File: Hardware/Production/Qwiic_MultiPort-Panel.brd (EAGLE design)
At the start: 149.1 x 143.3 mm, 606 parts, among them J1 QWIIC_RIGHT_ANGLE, J10 QWIIC_RIGHT_ANGLE, J100 QWIIC_RIGHT_ANGLE, J11 QWIIC_RIGHT_ANGLE, J12 QWIIC_RIGHT_ANGLE, J13 QWIIC_RIGHT_ANGLE, J14 QWIIC_RIGHT_ANGLE, J15 QWIIC_RIGHT_ANGLE, J16 QWIIC_RIGHT_ANGLE, J17 QWIIC_RIGHT_ANGLE, J18 QWIIC_RIGHT_ANGLE, J19 QWIIC_RIGHT_ANGLE, J2 QWIIC_RIGHT_ANGLE, J20 QWIIC_RIGHT_ANGLE, J21 QWIIC_RIGHT_ANGLE, J22 QWIIC_RIGHT_ANGLE, J23 QWIIC_RIGHT_ANGLE, J24 QWIIC_RIGHT_ANGLE, J25 QWIIC_RIGHT_ANGLE, J26 QWIIC_RIGHT_ANGLE, J27 QWIIC_RIGHT_ANGLE, J28 QWIIC_RIGHT_ANGLE, J29 QWIIC_RIGHT_ANGLE, J3 QWIIC_RIGHT_ANGLE, J30 QWIIC_RIGHT_ANGLE, J31 QWIIC_RIGHT_ANGLE, J32 QWIIC_RIGHT_ANGLE, J33 QWIIC_RIGHT_ANGLE, J34 QWIIC_RIGHT_ANGLE, J35 QWIIC_RIGHT_ANGLE, J36 QWIIC_RIGHT_ANGLE, J37 QWIIC_RIGHT_ANGLE, J38 QWIIC_RIGHT_ANGLE, J39 QWIIC_RIGHT_ANGLE, J4 QWIIC_RIGHT_ANGLE, J40 QWIIC_RIGHT_ANGLE, J41 QWIIC_RIGHT_ANGLE, J42 QWIIC_RIGHT_ANGLE, J43 QWIIC_RIGHT_ANGLE, J44 QWIIC_RIGHT_ANGLE, J45 QWIIC_RIGHT_ANGLE, J46 QWIIC_RIGHT_ANGLE, J47 QWIIC_RIGHT_ANGLE, J48 QWIIC_RIGHT_ANGLE, J49 QWIIC_RIGHT_ANGLE, J5 QWIIC_RIGHT_ANGLE, J50 QWIIC_RIGHT_ANGLE, J51 QWIIC_RIGHT_ANGLE, J52 QWIIC_RIGHT_ANGLE, J53 QWIIC_RIGHT_ANGLE, J54 QWIIC_RIGHT_ANGLE, J55 QWIIC_RIGHT_ANGLE, J56 QWIIC_RIGHT_ANGLE, J57 QWIIC_RIGHT_ANGLE, J58 QWIIC_RIGHT_ANGLE, J59 QWIIC_RIGHT_ANGLE, J6 QWIIC_RIGHT_ANGLE, J60 QWIIC_RIGHT_ANGLE, J61 QWIIC_RIGHT_ANGLE, J62 QWIIC_RIGHT_ANGLE, J63 QWIIC_RIGHT_ANGLE, J64 QWIIC_RIGHT_ANGLE, J65 QWIIC_RIGHT_ANGLE, J66 QWIIC_RIGHT_ANGLE, J67 QWIIC_RIGHT_ANGLE, J68 QWIIC_RIGHT_ANGLE, J69 QWIIC_RIGHT_ANGLE, J7 QWIIC_RIGHT_ANGLE, J70 QWIIC_RIGHT_ANGLE, J71 QWIIC_RIGHT_ANGLE, J72 QWIIC_RIGHT_ANGLE, J73 QWIIC_RIGHT_ANGLE, J74 QWIIC_RIGHT_ANGLE, J75 QWIIC_RIGHT_ANGLE, J76 QWIIC_RIGHT_ANGLE, J77 QWIIC_RIGHT_ANGLE, J78 QWIIC_RIGHT_ANGLE, J79 QWIIC_RIGHT_ANGLE, J8 QWIIC_RIGHT_ANGLE, J80 QWIIC_RIGHT_ANGLE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

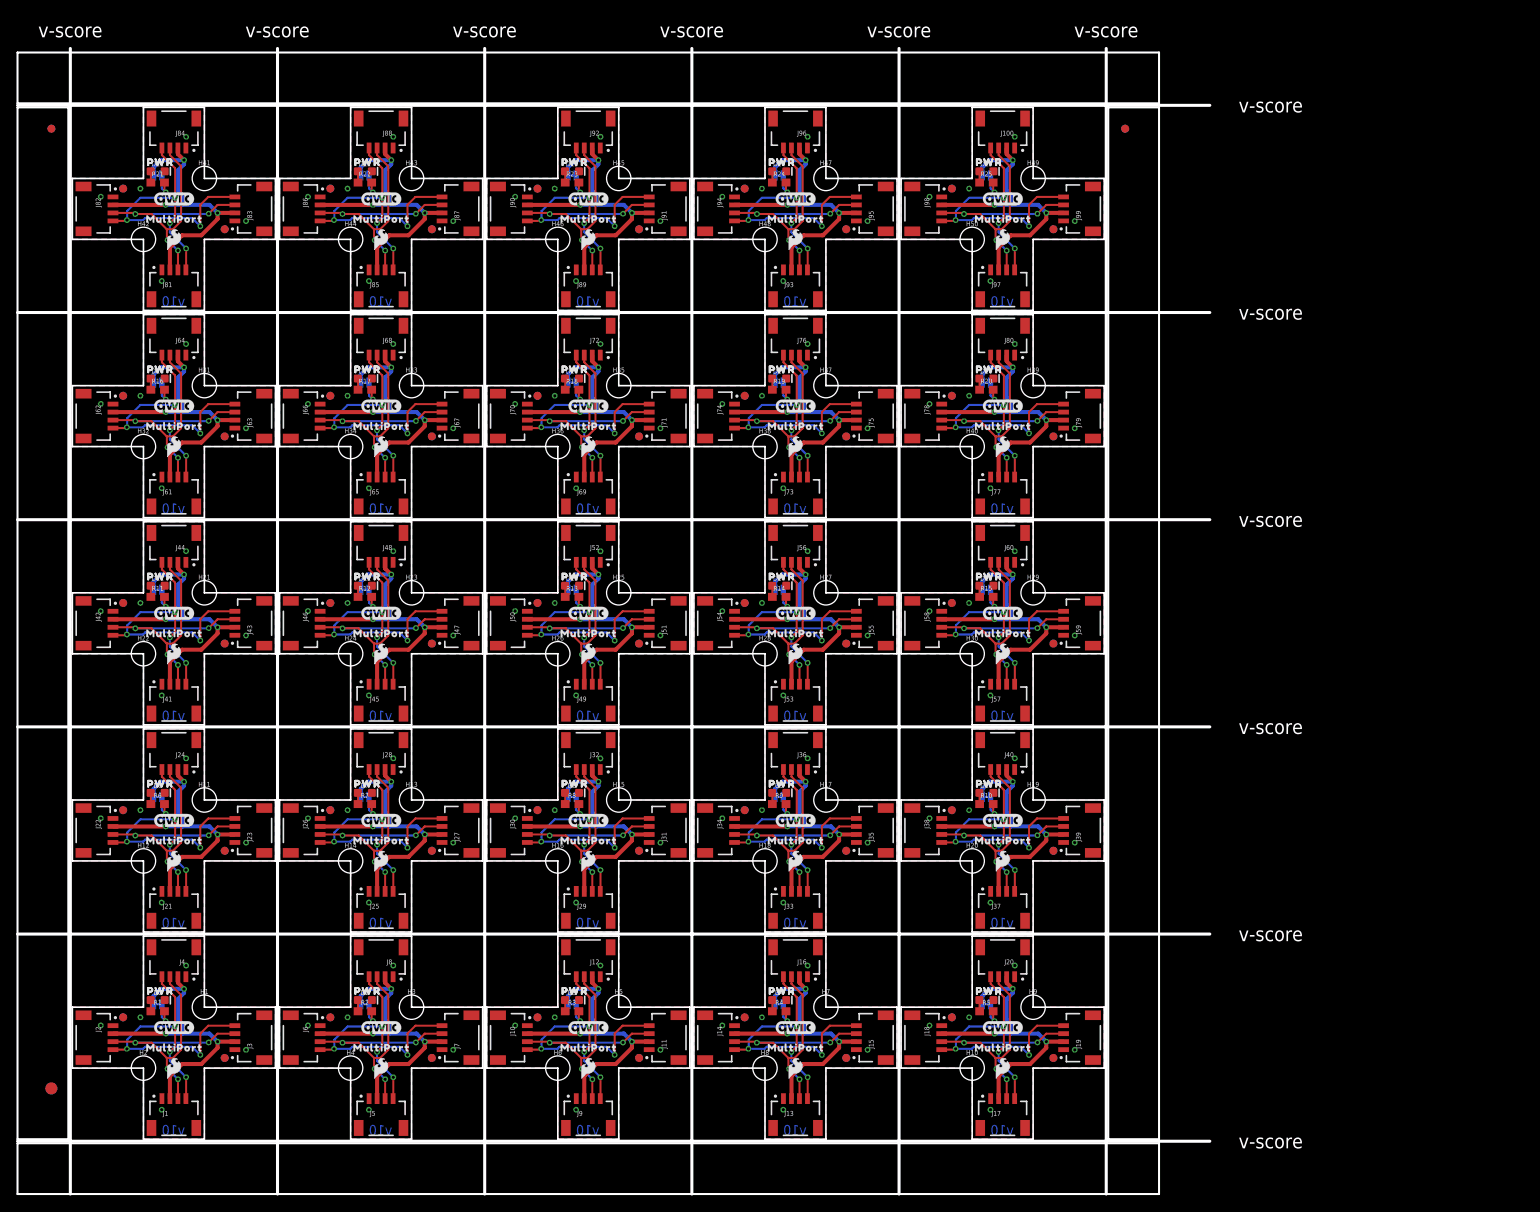
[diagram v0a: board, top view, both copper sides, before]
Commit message: MultiPort - re-panelized
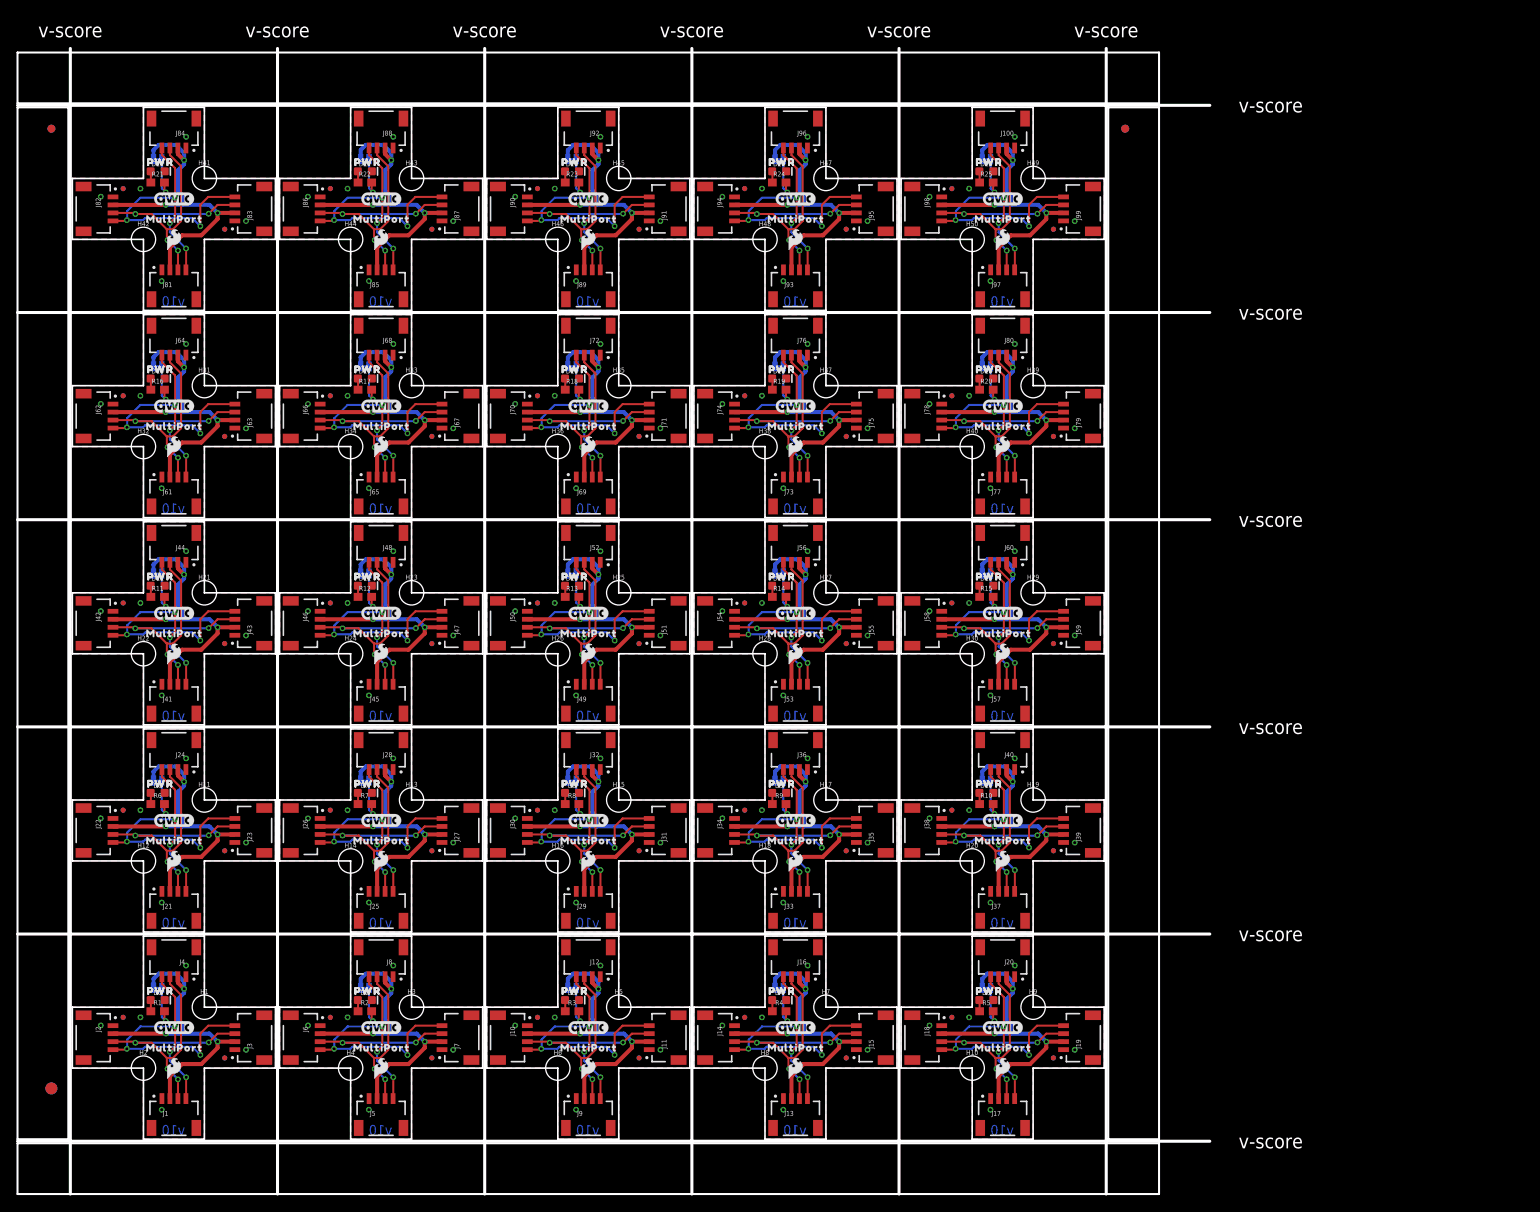
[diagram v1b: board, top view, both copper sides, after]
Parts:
- FD1, FD10, FD100, FD11, FD12, FD13, FD14, FD15, FD16, FD17, FD18, FD19, FD2, FD20, FD21, FD22, FD23, FD24, FD25, FD26, FD27, FD28, FD29, FD3, FD30, FD31, FD32, FD33, FD34, FD35, FD36, FD37, FD38, FD39, FD4, FD40, FD41, FD42, FD43, FD44, FD45, FD46, FD47, FD48, FD49, FD5, FD50, FD51, FD52, FD53, FD54, FD55, FD56, FD57, FD58, FD59, FD6, FD60, FD61, FD62, FD63, FD64, FD65, FD66, FD67, FD68, FD69, FD7, FD70, FD71, FD72, FD73, FD74, FD75, FD76, FD77, FD78, FD79, FD8, FD80, FD81, FD82, FD83, FD84, FD85, FD86, FD87, FD88, FD89, FD9, FD90, FD91, FD92, FD93, FD94, FD95, FD96, FD97, FD98, FD99: value FIDUCIAL1X2 -> FIDUCIALUFIDUCIAL; device SparkFun-Aesthetics:FIDUCIAL-1X2 -> SparkFun-Aesthetics:FIDUCIAL-MICRO
- U$104, U$111, U$118, U$12, U$125, U$132, U$139, U$146, U$153, U$160, U$167, U$174, U$20, U$27, U$34, U$41, U$48, U$55, U$62, U$69, U$76, U$83, U$90, U$97: device output:PWR0 -> output:MULTIPORT0
- U$105, U$112, U$119, U$126, U$133, U$14, U$140, U$147, U$154, U$161, U$168, U$175, U$21, U$28, U$35, U$42, U$49, U$56, U$63, U$70, U$77, U$84, U$91, U$98: device output:MULTIPORT0 -> output:#PWR#0
- U$3: device output:PWR0 -> SparkFun-Aesthetics:SFE_LOGO_FLAME_.1
- U$5: device SparkFun-Aesthetics:SFE_LOGO_FLAME_.1 -> output:#PWR#0
- moved U$3 27.4 mm to (38.6, 8.89), flipped to the top
- moved U$5 25.1 mm to (15.6, 18.9), flipped to the bottom
- moved U$119 10.3 mm to (41.5, 96.6), flipped to the bottom
- moved U$154 10.3 mm to (41.5, 122.6), flipped to the bottom
- moved U$112 10.3 mm to (15.6, 96.6), flipped to the bottom
- moved U$147 10.3 mm to (15.6, 122.6), flipped to the bottom
- moved U$126 10.3 mm to (67.4, 96.6), flipped to the bottom
- moved U$133 10.3 mm to (93.3, 96.6), flipped to the bottom
- moved U$140 10.3 mm to (119.3, 96.6), flipped to the bottom
- moved U$161 10.3 mm to (67.4, 122.6), flipped to the bottom
- moved U$168 10.3 mm to (93.3, 122.6), flipped to the bottom
- moved U$175 10.3 mm to (119.3, 122.6), flipped to the bottom
- moved U$49 10.3 mm to (41.5, 44.8), flipped to the bottom
- moved U$84 10.3 mm to (41.5, 70.7), flipped to the bottom
- moved U$42 10.3 mm to (15.6, 44.8), flipped to the bottom
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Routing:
- net N$50: track 3.63 -> 5.66 mm
- net N$48: track 3.63 -> 5.66 mm
- net N$46: track 3.63 -> 5.66 mm
- net N$44: track 3.63 -> 5.66 mm
- net N$42: track 3.63 -> 5.66 mm
- net N$40: track 3.63 -> 5.66 mm
- net N$38: track 3.63 -> 5.66 mm
- net N$36: track 3.63 -> 5.66 mm
- net N$34: track 3.63 -> 5.66 mm
- net N$32: track 3.63 -> 5.66 mm
- net N$30: track 3.63 -> 5.66 mm
- net N$28: track 3.63 -> 5.66 mm
- net N$26: track 3.63 -> 5.66 mm
- net N$24: track 3.63 -> 5.66 mm
- net N$22: track 3.63 -> 5.66 mm
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
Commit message: Re-panelized Qwiic MultiPort
Less than 7x5 inches
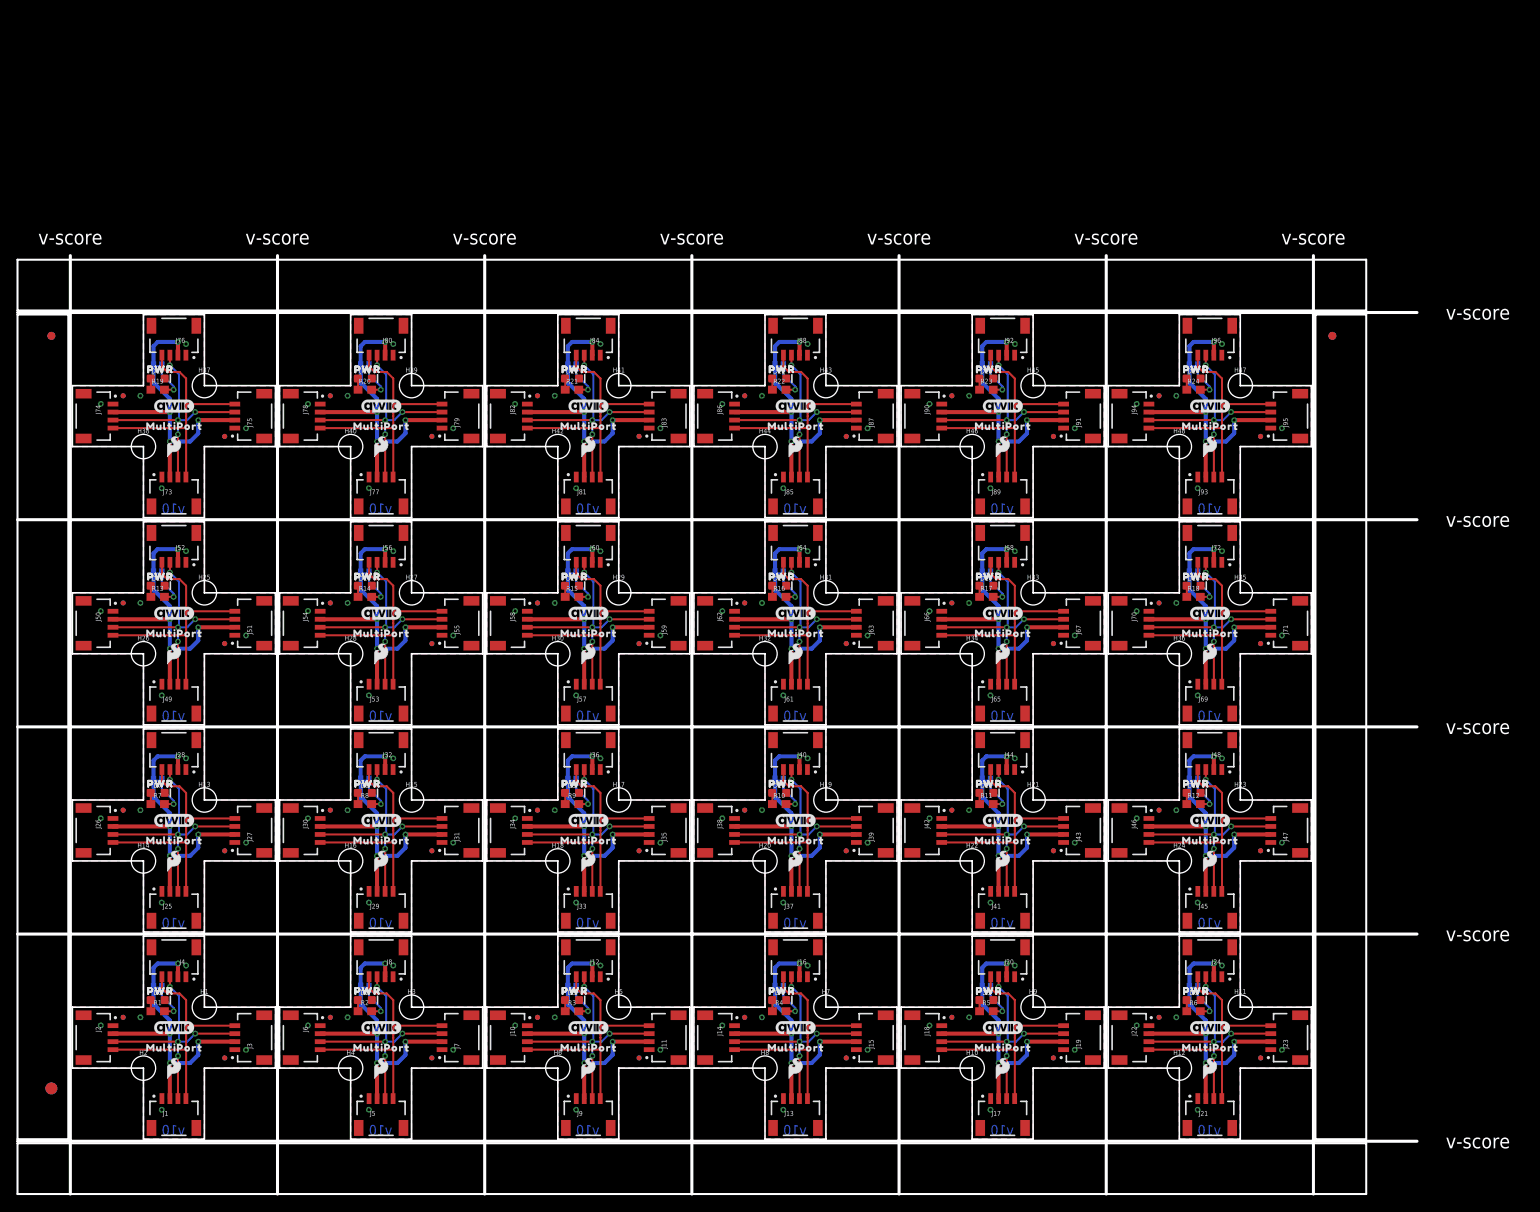
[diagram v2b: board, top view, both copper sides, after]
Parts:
- removed D25: RED, SparkFun-LED:LED-0603
- removed FD100, FD97, FD98, FD99: FIDUCIALUFIDUCIAL, SparkFun-Aesthetics:FIDUCIAL-MICRO
- removed H49, H50: STAND-OFFTIGHT, SparkFun-Hardware:STAND-OFF-TIGHT
- removed J100, J97, J98, J99: QWIIC_RIGHT_ANGLE, SparkFun-Connectors:JST04_1MM_RA
- removed JP25: PWR_LED, SparkFun-Jumpers:SMT-JUMPER_2_NC_TRACE_SILK
- removed LOGO100: SFE_LOGO_NAME.2_INCH, SparkFun-Aesthetics:SFE_LOGO_NAME_.2
- removed LOGO97, LOGO98: QWIIC_LOGO_5MM, SparkFun-Aesthetics:QWIIC_5MM
- removed LOGO99: OSHW-LOGOS, SparkFun-Aesthetics:OSHW-LOGO-S
- removed R25: 1k, SparkFun-Resistors:0603
- removed U$169: (no value), SparkFun-Aesthetics:SFE_LOGO_FLAME_.1
- removed U$170, U$173: (no value), output:PWR0
- removed U$171: (no value), output:MULTI0
- removed U$172: (no value), output:PORT0
- removed U$174: (no value), output:MULTIPORT0
- removed U$175: (no value), output:#PWR#0
- moved H11 132.1 mm to (146.1, 16.5)
- moved H12 132.1 mm to (138.4, 8.89)
- moved J21 132.1 mm to (142.2, 5.08)
- moved J23 132.1 mm to (149.9, 12.7)
- moved J24 132.1 mm to (142.2, 20.3)
- moved LOGO21 132.1 mm to (142.2, 14.0)
- moved LOGO22 132.1 mm to (142.2, 7.62)
- moved LOGO23 132.1 mm to (142.2, 22.9)
- moved LOGO24 132.1 mm to (142.2, 12.7)
- moved U$36 132.1 mm to (142.2, 8.89)
- moved U$39 132.1 mm to (144.5, 2.79)
- moved U$41 132.1 mm to (138.0, 11.4)
- moved D6 132.1 mm to (140.2, 17.4)
- moved FD21 132.1 mm to (135.9, 15.2)
- moved FD22 132.1 mm to (135.9, 15.2)
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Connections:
- removed net 3.3V24: J100.2, J97.2, J98.2, J99.2, JP25.2
- removed net GND24: D25.C, J100.1, J97.1, J98.1, J99.1
- removed net N$49: D25.A, R25.1
- removed net N$50: JP25.1, R25.2
- removed net SCL24: J100.4, J97.4, J98.4, J99.4
- removed net SDA24: J100.3, J97.3, J98.3, J99.3
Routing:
- net SCL24: track 43.8 -> 0.00 mm, vias 5 -> 0
- net 3.3V24: track 41.2 -> 0.00 mm, vias 3 -> 0
- net SDA24: track 38.1 -> 0.00 mm, vias 4 -> 0
- net SCL9: track 43.8 -> 32.6 mm, vias 5 -> 0
- net SCL7: track 43.8 -> 32.6 mm, vias 5 -> 0
- net SCL15: track 43.8 -> 32.6 mm, vias 5 -> 0
- net SCL16: track 43.8 -> 32.6 mm, vias 5 -> 0
- net SCL6: track 43.8 -> 32.6 mm, vias 5 -> 0
- net SCL5: track 43.8 -> 32.6 mm, vias 5 -> 0
- net SCL8: track 43.8 -> 32.6 mm, vias 5 -> 0
- net SCL4: track 43.8 -> 32.6 mm, vias 5 -> 0
- net SCL3: track 43.8 -> 32.6 mm, vias 5 -> 0
- net SCL21: track 43.8 -> 32.6 mm, vias 5 -> 0
- net SCL19: track 43.8 -> 32.6 mm, vias 5 -> 0
- net SCL17: track 43.8 -> 32.6 mm, vias 5 -> 0
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- removed copper zone on layer 1, net GND24
- removed copper zone on layer 16, net GND24
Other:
- board size 149.1 x 143.3 mm -> 175 x 117.3 mm
